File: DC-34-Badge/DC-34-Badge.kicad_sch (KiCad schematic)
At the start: 81 parts, among them U1 ESP32-S3-MINI-1, U2 AP2112K-3.3

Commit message: Added labels for resistors and capacitors.
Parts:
- added R31: A9050, OptoDevice:R_LDR_5.0x4.1mm_P3mm_Vertical, symbol Sensor_Optical:A9050
- added R7: 10k, Resistor_SMD:R_0402_1005Metric, symbol Device:R
- gave numbers to parts that had none: 45
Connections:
- net +3.3V: now also R31.1
- net PHOTO: now reaches U1.22 (GPIO18/U1RXD/ADC2_CH7/CLK_OUT3)
- net PHOTO: now also R31.2, R7.2

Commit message: April 3 2026 Meeting
What was worked on in the Friday collaboration meeting.
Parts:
- gave numbers to parts that had none: 27
- renumbered D4 to D3
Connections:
- net GND: now also R7.1

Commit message: Added No-Connects to Schematic
Added no-connects to the schematic to address design rule checker findings.
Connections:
- net +3.3V: now also BZ1.2 (+), R31.2; no longer BZ1.1 (-), R31.1
- net PHOTO: now also R31.1; no longer R31.2
- net at Q1.2 (C), R30.1: now also BZ1.1 (-); no longer BZ1.2 (+)
- no-connect marks 0 -> 28
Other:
- moved on the sheet: R31
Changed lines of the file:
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@@
   (junction (at 264.16 64.77) (diameter 0) (color 0 0 0 0)
   )
-  (junction (at 39.37 88.9) (diameter 0) (color 0 0 0 0)
-  )
   (junction (at 92.71 31.75) (diameter 0) (color 0 0 0 0)
   )
@@
   (junction (at 232.41 107.95) (diameter 0) (color 0 0 0 0)
   )
+  (junction (at 39.37 88.9) (diameter 0) (color 0 0 0 0)
+  )
   (junction (at 87.63 176.53) (diameter 0) (color 0 0 0 0)
   )
@@
   (junction (at 97.79 176.53) (diameter 0) (color 0 0 0 0)
   )
+  (no_connect (at 53.34 154.94))
+  (no_connect (at 266.7 39.37))
+  (no_connect (at 143.51 88.9))
+  (no_connect (at 143.51 132.08))
+  (no_connect (at 52.07 81.28))
+  (no_connect (at 173.99 76.2))
+  (no_connect (at 138.43 35.56))
+  (no_connect (at 52.07 73.66))
+  (no_connect (at 143.51 66.04))
+  (no_connect (at 231.14 39.37))
+  (no_connect (at 143.51 127))
+  (no_connect (at 52.07 71.12))
+  (no_connect (at 52.07 124.46))
+  (no_connect (at 143.51 68.58))
+  (no_connect (at 143.51 124.46))
+  (no_connect (at 52.07 127))
+  (no_connect (at 115.57 176.53))
+  (no_connect (at 52.07 83.82))
+  (no_connect (at 138.43 30.48))
+  (no_connect (at 52.07 78.74))
+  (no_connect (at 266.7 26.67))
+  (no_connect (at 209.55 68.58))
+  (no_connect (at 138.43 40.64))
+  (no_connect (at 266.7 34.29))
+  (no_connect (at 52.07 86.36))
+  (no_connect (at 143.51 134.62))
+  (no_connect (at 128.27 38.1))
+  (no_connect (at 143.51 129.54))
   (wire (pts (xy 177.8 36.83) (xy 177.8 44.45))
     (stroke (width 0) (type default) (color 0 0 0 0))
@@
     (stroke (width 0) (type default) (color 0 0 0 0))
   )
-  (wire (pts (xy 39.37 76.2) (xy 39.37 78.74))
-    (stroke (width 0) (type default) (color 0 0 0 0))
-  )
   (wire (pts (xy 118.11 168.91) (xy 118.11 176.53))
     (stroke (width 0) (type default) (color 0 0 0 0))
@@
     (stroke (width 0) (type default) (color 0 0 0 0))
   )
-  (wire (pts (xy 39.37 86.36) (xy 39.37 88.9))
-    (stroke (width 0) (type default) (color 0 0 0 0))
-  )
   (wire (pts (xy 264.16 119.38) (xy 265.43 119.38))
     (stroke (width 0) (type default) (color 0 0 0 0))
@@
     (stroke (width 0) (type default) (color 0 0 0 0))
   )
-  (wire (pts (xy 29.21 67.31) (xy 29.21 68.58))
-    (stroke (width 0) (type default) (color 0 0 0 0))
-  )
   (wire (pts (xy 234.95 62.23) (xy 234.95 64.77))
     (stroke (width 0) (type default) (color 0 0 0 0))
@@
     (stroke (width 0) (type default) (color 0 0 0 0))
   )
+  (wire (pts (xy 39.37 76.2) (xy 39.37 78.74))
+    (stroke (width 0) (type default) (color 0 0 0 0))
+  )
   (wire (pts (xy 227.33 90.17) (xy 224.79 90.17))
     (stroke (width 0) (type default) (color 0 0 0 0))
@@
     (stroke (width 0) (type default) (color 0 0 0 0))
   )
+  (wire (pts (xy 29.21 67.31) (xy 29.21 68.58))
+    (stroke (width 0) (type default) (color 0 0 0 0))
+  )
   (wire (pts (xy 49.53 152.4) (xy 53.34 152.4))
     (stroke (width 0) (type default) (color 0 0 0 0))
@@
     (stroke (width 0) (type default) (color 0 0 0 0))
   )
+  (wire (pts (xy 29.21 60.96) (xy 29.21 62.23))
+    (stroke (width 0) (type default) (color 0 0 0 0))
+  )
   (wire (pts (xy 163.83 68.58) (xy 163.83 86.36))
     (stroke (width 0) (type default) (color 0 0 0 0))
@@
     (stroke (width 0) (type default) (color 0 0 0 0))
   )
-  (wire (pts (xy 29.21 62.23) (xy 29.21 60.96))
-    (stroke (width 0) (type default) (color 0 0 0 0))
-  )
   (wire (pts (xy 160.02 177.8) (xy 160.02 195.58))
     (stroke (width 0) (type default) (color 0 0 0 0))
@@
     (stroke (width 0) (type default) (color 0 0 0 0))
   )
+  (wire (pts (xy 39.37 86.36) (xy 39.37 88.9))
+    (stroke (width 0) (type default) (color 0 0 0 0))
+  )
   (wire (pts (xy 49.53 157.48) (xy 49.53 158.75))
     (stroke (width 0) (type default) (color 0 0 0 0))
@@
     (pin "1")
   )
-  (symbol (lib_id "Device:Buzzer") (at 31.75 64.77 0) (unit 1)
+  (symbol (lib_id "Device:Buzzer") (at 31.75 64.77 0) (mirror x) (unit 1)
     (in_bom yes) (on_board yes) (fields_autoplaced)
-    (property "Reference" "BZ1" (id 0) (at 35.56 63.4999 0)
-      (effects (font (size 1.27 1.27)) (justify left))
-    )
-    (property "Value" "Buzzer" (id 1) (at 35.56 66.0399 0)
-      (effects (font (size 1.27 1.27)) (justify left))
-    )
-    (property "Footprint" "Diode_THT:D_A-405_P5.08mm_Vertical_AnodeUp" (id 2) (at 31.115 62.23 90)
+    (property "Reference" "BZ1" (id 0) (at 32.512 55.88 0))
+    (property "Value" "Buzzer" (id 1) (at 32.512 58.42 0))
+    (property "Footprint" "Diode_THT:D_A-405_P5.08mm_Vertical_AnodeUp" (id 2) (at 31.115 67.31 90)
       (effects (font (size 1.27 1.27)) hide)
     )
-    (property "Datasheet" "~" (id 3) (at 31.115 62.23 90)
+    (property "Datasheet" "~" (id 3) (at 31.115 67.31 90)
       (effects (font (size 1.27 1.27)) hide)
     )
@@
     (pin "1")
   )
-  (symbol (lib_id "Sensor_Optical:A9050") (at 39.37 82.55 0) (unit 1)
+  (symbol (lib_id "Sensor_Optical:A9050") (at 39.37 82.55 180) (unit 1)
     (in_bom yes) (on_board yes) (fields_autoplaced)
-    (property "Reference" "R31" (id 0) (at 41.91 81.2799 0)
-      (effects (font (size 1.27 1.27)) (justify left))
+    (property "Reference" "R31" (id 0) (at 44.45 81.2799 0)
+      (effects (font (size 1.27 1.27)) (justify right))
     )
-    (property "Value" "A9050" (id 1) (at 41.91 83.8199 0)
-      (effects (font (size 1.27 1.27)) (justify left))
+    (property "Value" "A9050" (id 1) (at 44.45 83.8199 0)
+      (effects (font (size 1.27 1.27)) (justify right))
     )
-    (property "Footprint" "OptoDevice:R_LDR_5.0x4.1mm_P3mm_Vertical" (id 2) (at 43.815 82.55 90)
+    (property "Footprint" "OptoDevice:R_LDR_5.0x4.1mm_P3mm_Vertical" (id 2) (at 34.925 82.55 90)
       (effects (font (size 1.27 1.27)) hide)
     )
-    (property "Datasheet" "http://cdn-reichelt.de/documents/datenblatt/A500/A90xxxx%23PE.pdf" (id 3) (at 39.37 83.82 0)
+    (property "Datasheet" "http://cdn-reichelt.de/documents/datenblatt/A500/A90xxxx%23PE.pdf" (id 3) (at 39.37 81.28 0)
       (effects (font (size 1.27 1.27)) hide)
     )

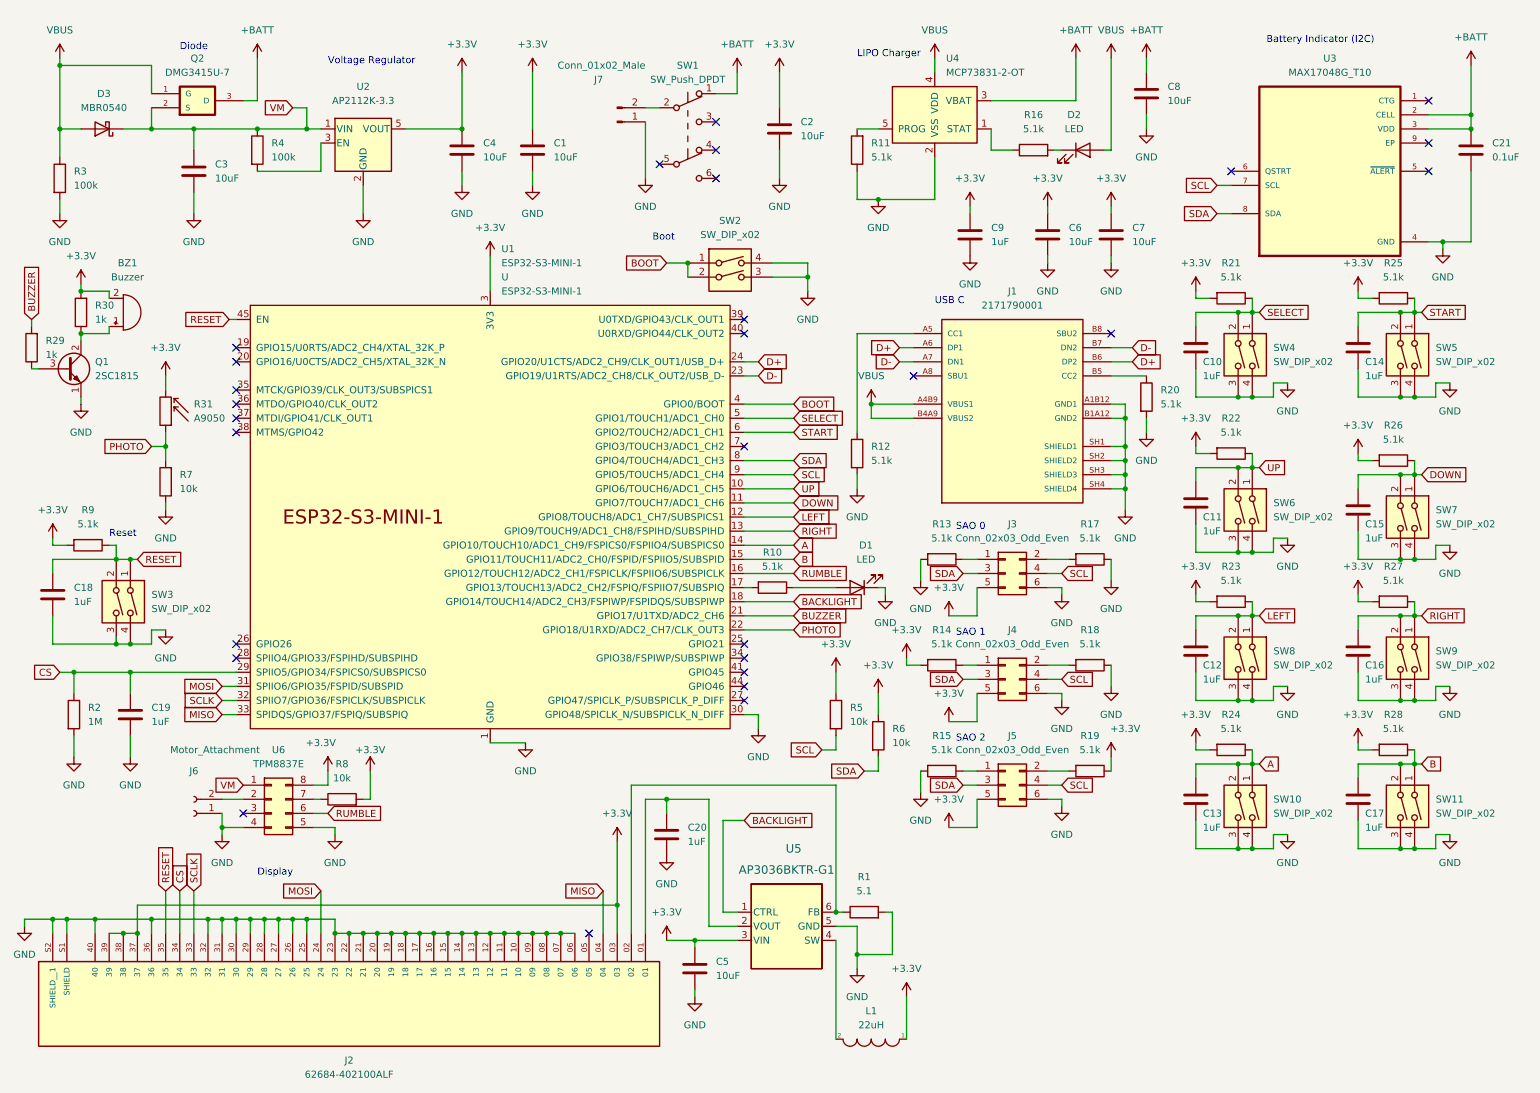
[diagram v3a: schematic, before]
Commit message: Removed design errors from schematic.
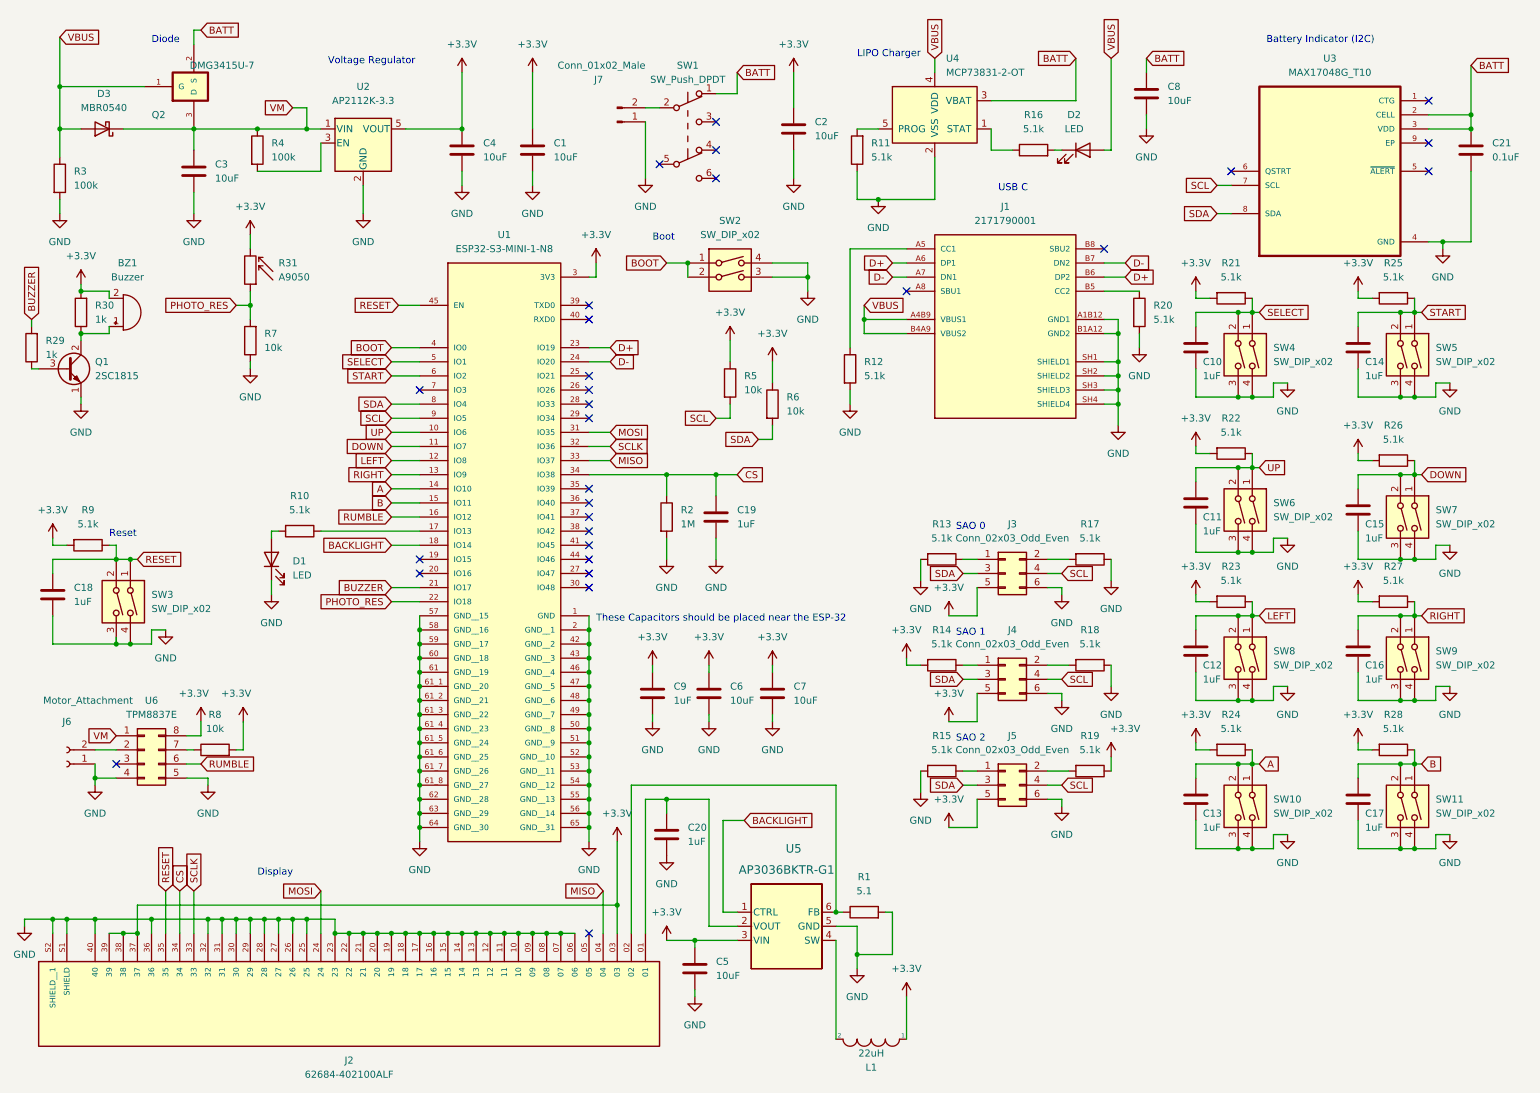
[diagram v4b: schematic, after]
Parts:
- removed U1: ESP32-S3-MINI-1, Espressif:ESP32-S3-MINI-1U, symbol Espressif:ESP32-S3-MINI-1
- added U1: ESP32-S3-MINI-1-N8, expressif-digikey:XCVR_ESP32-S3-MINI-1-N8, symbol ESP32-S3-MINI-1-N8:ESP32-S3-MINI-1-N8
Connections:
- net +3.3V: now also U1.3 (3V3)
- net A: now also U1.14 (IO10)
- net B: now also U1.15 (IO11)
- net BACKLIGHT: now also U1.18 (IO14)
- net BOOT: now also U1.4 (IO0)
- net BUZZER: now also U1.21 (IO17)
- net CS: now also U1.34 (IO38)
- net D+: now also U1.23 (IO19)
- net D-: now also U1.24 (IO20)
- net DOWN: now also U1.11 (IO7)
- net GND: now also U1.1 (GND), U1.2 (GND__1), U1.42 (GND__2), U1.43 (GND__3), U1.46 (GND__4), U1.47 (GND__5), U1.48 (GND__6), U1.49 (GND__7), U1.50 (GND__8), U1.51 (GND__9), U1.52 (GND__10), U1.53 (GND__11), U1.54 (GND__12), U1.55 (GND__13), U1.56 (GND__14), U1.57 (GND__15), U1.58 (GND__16), U1.59 (GND__17), U1.60 (GND__18), U1.61 (GND__19), U1.61_1 (GND__20), U1.61_2 (GND__21), U1.61_3 (GND__22), U1.61_4 (GND__23), U1.61_5 (GND__24), U1.61_6 (GND__25), U1.61_7 (GND__26), U1.61_8 (GND__27), U1.62 (GND__28), U1.63 (GND__29), U1.64 (GND__30), U1.65 (GND__31)
- net LEFT: now also U1.12 (IO8)
- net MISO: now also U1.33 (IO37)
- net MOSI: now also U1.31 (IO35)
- net RESET: now also U1.45 (EN)
- net RIGHT: now also U1.13 (IO9)
- net RUMBLE: now also U1.16 (IO12)
- net SCL: now also U1.9 (IO5)
- net SCLK: now also U1.32 (IO36)
- net SDA: now also U1.8 (IO4)
- net SELECT: now also U1.5 (IO1)
- net START: now also U1.6 (IO2)
- net UP: now also U1.10 (IO6)
- net VM: now also Q2.3 (D); no longer Q2.2 (S)
- net at R10.2: now also D1.2 (A)
- net at R10.1: now also U1.17 (IO13); no longer D1.2 (A)
- net +BATT renamed BATT
- net BATT: now also Q2.2 (S); no longer Q2.3 (D)
- net PHOTO renamed PHOTO_RES
- net PHOTO_RES: now also U1.22 (IO18)
- no-connect marks 28 -> 29
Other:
- note added: "These Capacitors should be placed near the ESP-32"
- moved on the sheet: C19, C2, C6, C7, C9, J1, J6, Q2, R12, R2, R20, R31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

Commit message: Added footprint libraries and placed componets.
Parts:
- J7: footprint (none) -> Connector_JST:JST_XH_B2B-XH-AM_1x02_P2.50mm_Vertical
- Q2: footprint DMG3415U-7:SOT95P240X105-3N -> DMG3415U_7:SOT95P240X105-3N
- U3: footprint MAX17048G_T10:SON50P200X200X80-9N -> MAX17048G:SON50P200X200X80-9N
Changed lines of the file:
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@@
     (property "Reference" "Q2" (id 0) (at 38.1 29.21 0))
     (property "Value" "DMG3415U-7" (id 1) (at 49.53 20.32 0))
-    (property "Footprint" "DMG3415U-7:SOT95P240X105-3N" (id 2) (at 46.99 30.48 0)
+    (property "Footprint" "DMG3415U_7:SOT95P240X105-3N" (id 2) (at 46.99 30.48 0)
       (effects (font (size 1.27 1.27)) (justify bottom) hide)
     )
@@
       (effects (font (size 1.27 1.27)) (justify right))
     )
-    (property "Footprint" "" (id 2) (at 120.65 30.48 0)
+    (property "Footprint" "Connector_JST:JST_XH_B2B-XH-AM_1x02_P2.50mm_Vertical" (id 2) (at 120.65 30.48 0)
       (effects (font (size 1.27 1.27)) hide)
     )
@@
     (property "Reference" "U3" (id 0) (at 248.92 19.05 0))
     (property "Value" "MAX17048G_T10" (id 1) (at 248.92 21.59 0))
-    (property "Footprint" "MAX17048G_T10:SON50P200X200X80-9N" (id 2) (at 248.92 39.37 0)
+    (property "Footprint" "MAX17048G:SON50P200X200X80-9N" (id 2) (at 248.92 39.37 0)
       (effects (font (size 1.27 1.27)) (justify bottom) hide)
     )
@@
     )
     (path "/d8e38930-1f5d-44a9-8e36-73d2153ecfed"
-      (reference "J7") (unit 1) (value "Conn_01x02_Male") (footprint "")
+      (reference "J7") (unit 1) (value "Conn_01x02_Male") (footprint "Connector_JST:JST_XH_B2B-XH-AM_1x02_P2.50mm_Vertical")
     )
     (path "/84612367-def9-41be-aabe-b399004cf88a"
@@
     )
     (path "/afd96db4-7e2e-4b67-adcc-d2d9a8fdf055"
-      (reference "Q2") (unit 1) (value "DMG3415U-7") (footprint "DMG3415U-7:SOT95P240X105-3N")
+      (reference "Q2") (unit 1) (value "DMG3415U-7") (footprint "DMG3415U_7:SOT95P240X105-3N")
     )
     (path "/63c487d9-1b6c-46a7-925c-77e22803c4af"
@@
     )
     (path "/e7f65285-5ba0-4b55-a2bc-7867db0a223e"
-      (reference "U3") (unit 1) (value "MAX17048G_T10") (footprint "MAX17048G_T10:SON50P200X200X80-9N")
+      (reference "U3") (unit 1) (value "MAX17048G_T10") (footprint "MAX17048G:SON50P200X200X80-9N")
     )
     (path "/da558b23-ef67-4430-852a-28e996899834"
